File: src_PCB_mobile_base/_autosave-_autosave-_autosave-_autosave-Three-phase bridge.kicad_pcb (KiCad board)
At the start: 2 copper layers, 401.6 x 318 mm, 105 parts, among them M1 MCP6022-I/P, M2 MCP6022-I/P, P1 CONN_1, P10 CONN_1, P11 CONN_1, P12 CONN_1, P13 CONN_1, P2 POWER_FUSE, P3 CONN_2, P4 CONN_1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

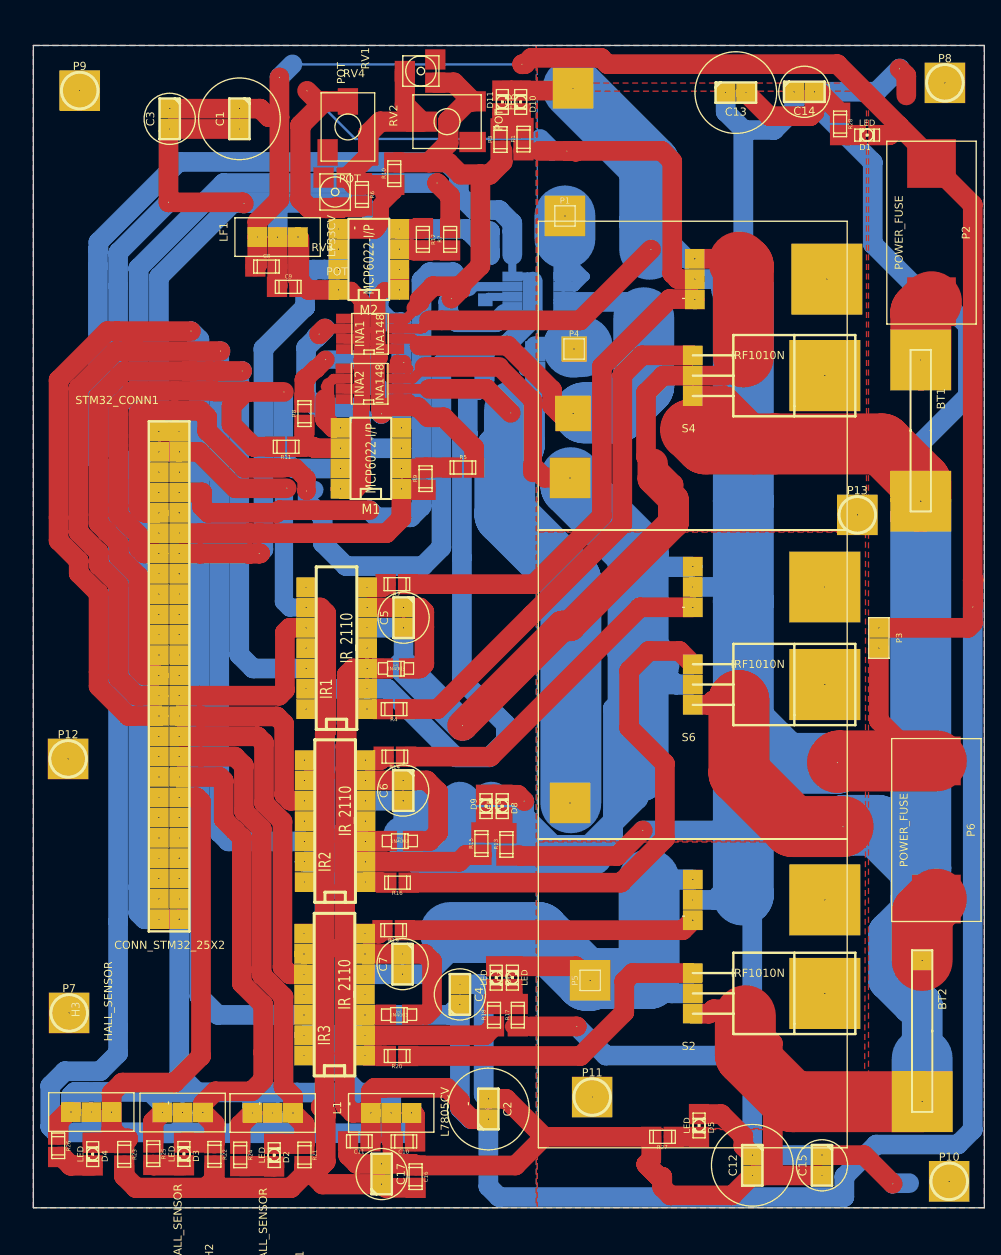
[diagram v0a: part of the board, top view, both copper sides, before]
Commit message: Modulos originales de libreria de Sebastian
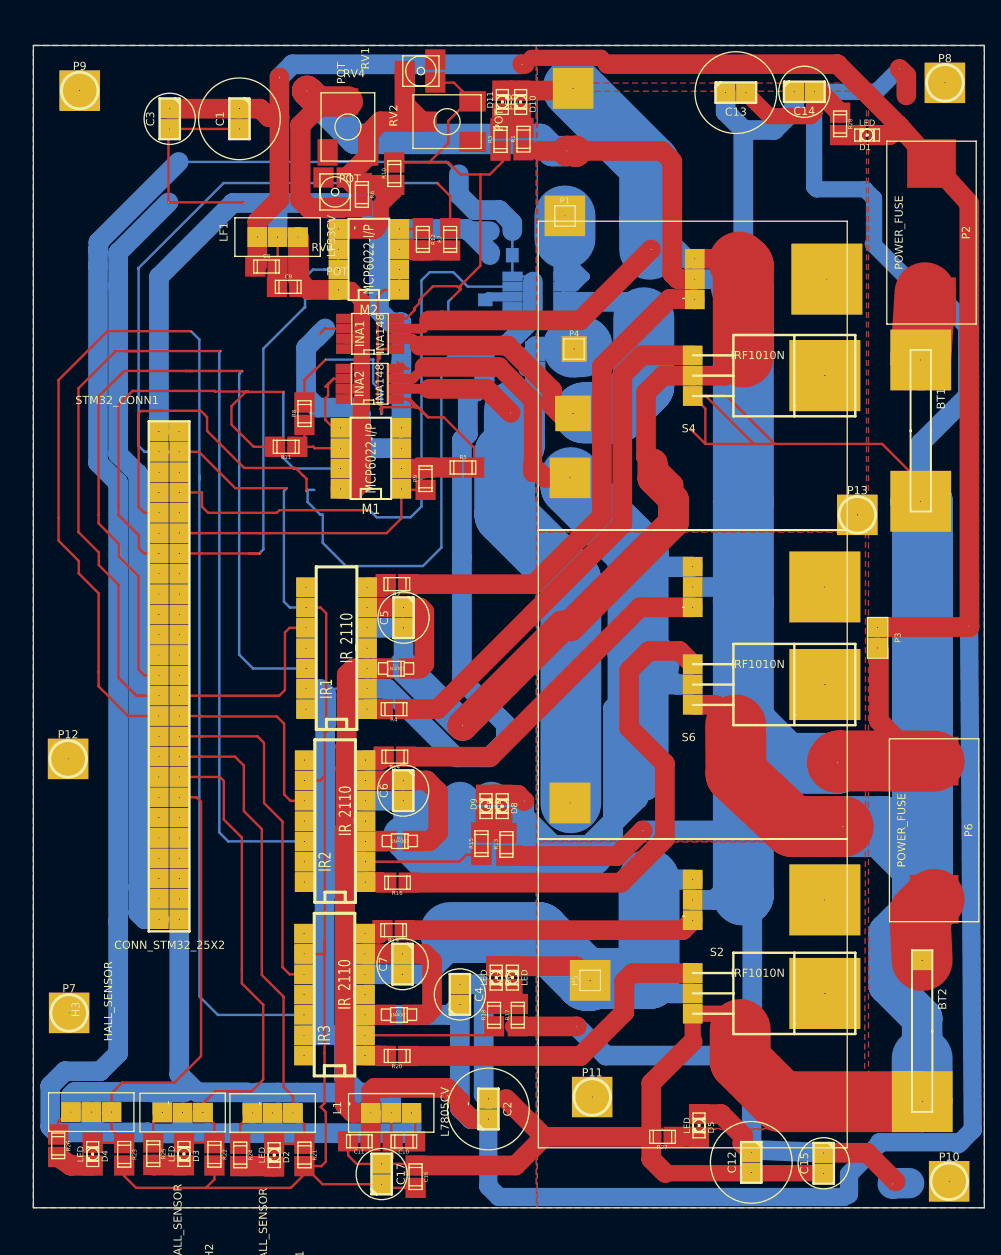
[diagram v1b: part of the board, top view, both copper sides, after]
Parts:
- moved C12 0.39 mm to (246.7, 204.1)
- moved C15 0.33 mm to (255.8, 204.2)
- moved P6 0.28 mm to (269.6, 162.6)
- moved P3 0.16 mm to (262.5, 138.6)
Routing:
- net GND: track 1061.5 -> 1139.1 mm
- net VCC: track 499.6 -> 493.3 mm
- net +48V: track 408.2 -> 409.2 mm
- net N-0000014: track 7.85 -> 8.43 mm
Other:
- net class 12 mil removed
- net class pista12mm added: clearance 0.254, trace_width 0.3048, via_dia 0.127, via_drill 0.1016
